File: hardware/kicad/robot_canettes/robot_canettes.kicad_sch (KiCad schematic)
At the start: 0 parts

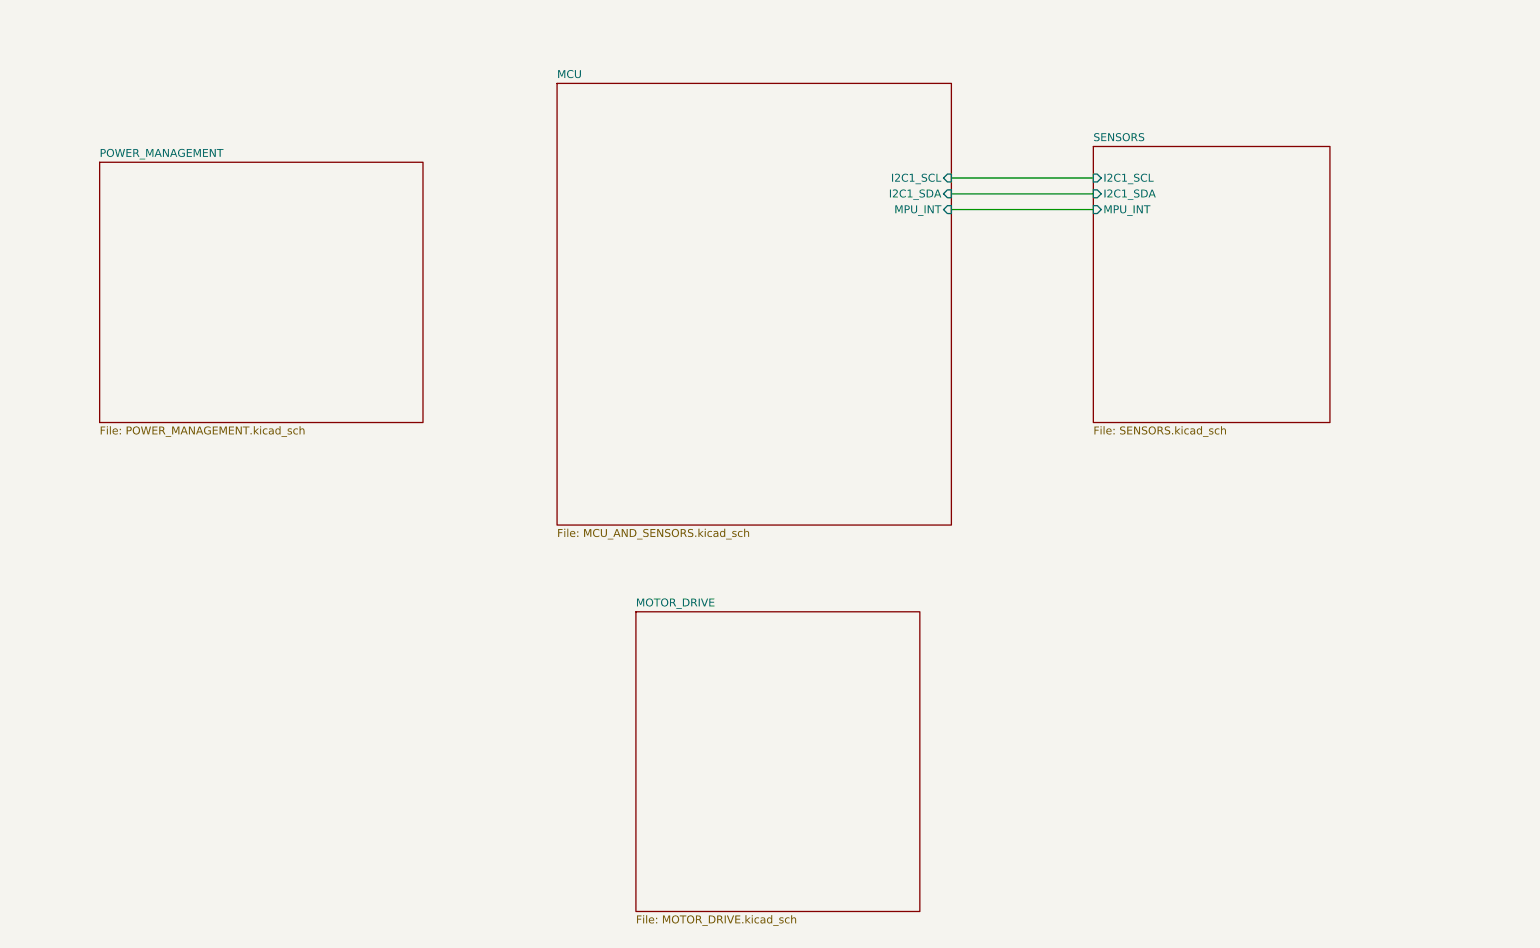
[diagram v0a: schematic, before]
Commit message: MAJ schema MCU/sensors
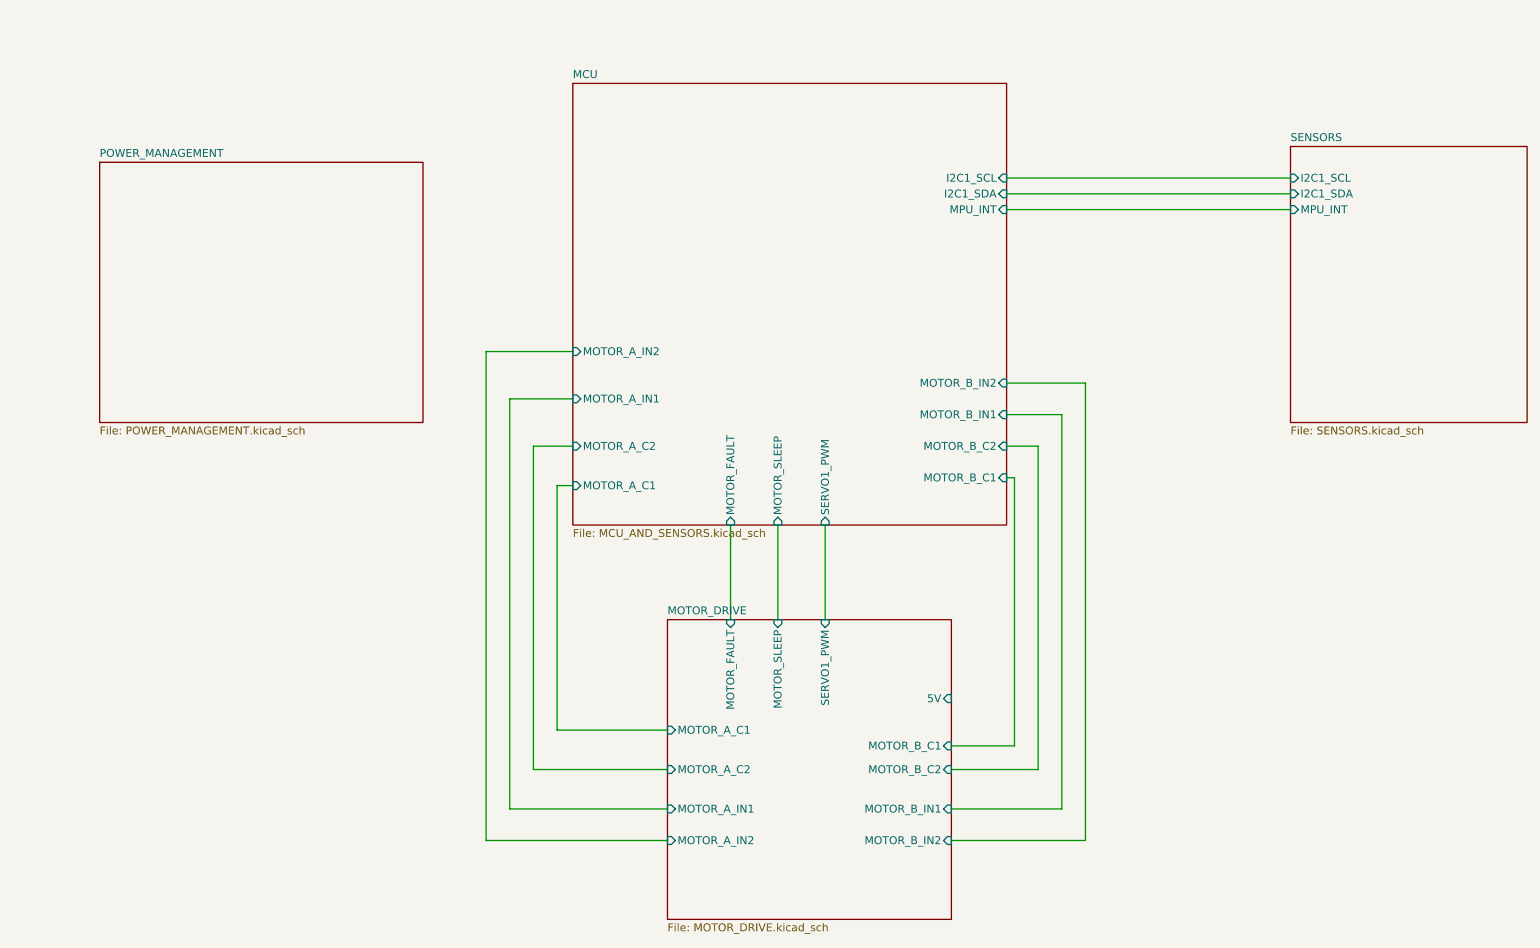
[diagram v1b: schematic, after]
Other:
- sheet MCU ports: added MOTOR_A_C1, MOTOR_A_C2, MOTOR_A_IN1, MOTOR_A_IN2, MOTOR_B_C1, MOTOR_B_C2, MOTOR_B_IN1, MOTOR_B_IN2, MOTOR_FAULT, MOTOR_SLEEP, SERVO1_PWM; removed none
- sheet MOTOR_DRIVE ports: added 5V, MOTOR_A_C1, MOTOR_A_C2, MOTOR_A_IN1, MOTOR_A_IN2, MOTOR_B_C1, MOTOR_B_C2, MOTOR_B_IN1, MOTOR_B_IN2, MOTOR_FAULT, MOTOR_SLEEP, SERVO1_PWM; removed none

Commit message: MAJ connecteur TOF2 (J10) et resistances pull-up
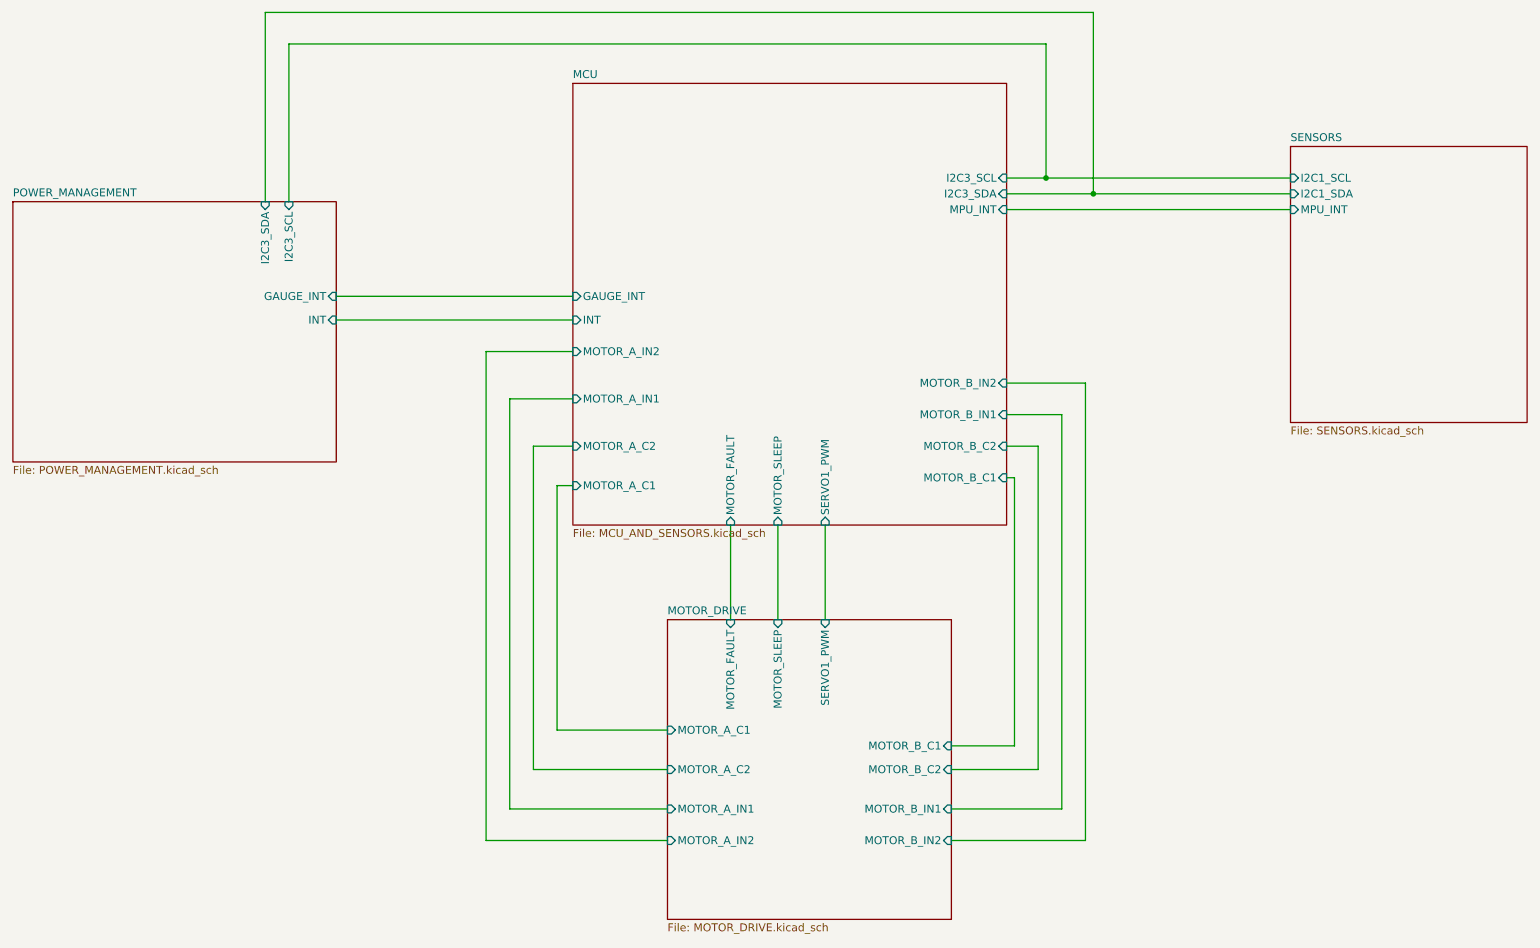
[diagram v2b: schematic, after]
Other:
- sheet MCU ports: added GAUGE_INT, I2C3_SCL, I2C3_SDA, INT; removed I2C1_SCL, I2C1_SDA
- sheet MOTOR_DRIVE ports: added none; removed 5V
- sheet POWER_MANAGEMENT ports: added GAUGE_INT, I2C3_SCL, I2C3_SDA, INT; removed none
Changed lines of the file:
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@@
 	(generator_version "10.0")
 	(paper "A4")
+	(junction
+		(at 205.74 46.99)
+		(diameter 0)
+		(color 0 0 0 0)
+	)
+	(junction
+		(at 198.12 44.45)
+		(diameter 0)
+		(color 0 0 0 0)
+	)
 	(wire
 		(pts
@@
 	(wire
 		(pts
+			(xy 76.2 48.26) (xy 76.2 22.86)
+		)
+		(stroke
+			(width 0)
+			(type default)
+		)
+	)
+	(wire
+		(pts
 			(xy 107.95 72.39) (xy 107.95 151.13)
 		)
@@
 	(wire
 		(pts
+			(xy 205.74 46.99) (xy 237.49 46.99)
+		)
+		(stroke
+			(width 0)
+			(type default)
+		)
+	)
+	(wire
+		(pts
+			(xy 83.82 63.5) (xy 121.92 63.5)
+		)
+		(stroke
+			(width 0)
+			(type default)
+		)
+	)
+	(wire
+		(pts
+			(xy 72.39 17.78) (xy 205.74 17.78)
+		)
+		(stroke
+			(width 0)
+			(type default)
+		)
+	)
+	(wire
+		(pts
 			(xy 154.94 100.33) (xy 154.94 115.57)
 		)
@@
 	(wire
 		(pts
+			(xy 198.12 44.45) (xy 237.49 44.45)
+		)
+		(stroke
+			(width 0)
+			(type default)
+		)
+	)
+	(wire
+		(pts
+			(xy 198.12 22.86) (xy 198.12 44.45)
+		)
+		(stroke
+			(width 0)
+			(type default)
+		)
+	)
+	(wire
+		(pts
 			(xy 121.92 87.63) (xy 115.57 87.63)
 		)
@@
 	(wire
 		(pts
+			(xy 72.39 48.26) (xy 72.39 17.78)
+		)
+		(stroke
+			(width 0)
+			(type default)
+		)
+	)
+	(wire
+		(pts
 			(xy 147.32 100.33) (xy 147.32 115.57)
 		)
@@
 	(wire
 		(pts
+			(xy 76.2 22.86) (xy 198.12 22.86)
+		)
+		(stroke
+			(width 0)
+			(type default)
+		)
+	)
+	(wire
+		(pts
 			(xy 121.92 93.98) (xy 119.38 93.98)
 		)
@@
 	(wire
 		(pts
+			(xy 205.74 17.78) (xy 205.74 46.99)
+		)
+		(stroke
+			(width 0)
+			(type default)
+		)
+	)
+	(wire
+		(pts
 			(xy 200.66 146.05) (xy 182.88 146.05)
 		)
@@
 	(wire
 		(pts
-			(xy 191.77 44.45) (xy 237.49 44.45)
+			(xy 191.77 44.45) (xy 198.12 44.45)
 		)
 		(stroke
@@
 	(wire
 		(pts
-			(xy 191.77 46.99) (xy 237.49 46.99)
+			(xy 191.77 46.99) (xy 205.74 46.99)
+		)
+		(stroke
+			(width 0)
+			(type default)
+		)
+	)
+	(wire
+		(pts
+			(xy 83.82 67.31) (xy 121.92 67.31)
 		)
 		(stroke
@@
 	)
 	(sheet
-		(at 45.72 41.91)
+		(at 31.75 48.26)
 		(size 52.07 41.91)
 		(exclude_from_sim no)
@@
 		)
 		(property "Sheetname" "POWER_MANAGEMENT"
-			(at 45.72 41.1984 0)
+			(at 31.75 47.5484 0)
 			(show_name no)
 			(do_not_autoplace no)
@@
 		)
 		(property "Sheetfile" "POWER_MANAGEMENT.kicad_sch"
-			(at 45.72 84.4046 0)
+			(at 31.75 90.7546 0)
 			(show_name no)
 			(do_not_autoplace no)
@@
 				)
 				(justify left top)
+			)
+		)
+		(pin "GAUGE_INT" input
+			(at 83.82 63.5 0)
+			(effects
+				(font
+					(size 1.27 1.27)
+				)
+				(justify right)
+			)
+		)
+		(pin "I2C3_SCL" input
+			(at 76.2 48.26 90)
+			(effects
+				(font
+					(size 1.27 1.27)
+				)
+				(justify right)
+			)
+		)
+		(pin "I2C3_SDA" input
+			(at 72.39 48.26 90)
+			(effects
+				(font
+					(size 1.27 1.27)
+				)
+				(justify right)
+			)
+		)
+		(pin "INT" input
+			(at 83.82 67.31 0)
+			(effects
+				(font
+					(size 1.27 1.27)
+				)
+				(justify right)
 			)
 		)
@@
 			)
 		)
-		(pin "I2C1_SCL" input
-			(at 191.77 44.45 0)
-			(effects
-				(font
-					(size 1.27 1.27)
-				)
-				(justify right)
-			)
-		)
-		(pin "I2C1_SDA" input
-			(at 191.77 46.99 0)
-			(effects
-				(font
-					(size 1.27 1.27)
-				)
-				(justify right)
-			)
-		)
 		(pin "MPU_INT" input
 			(at 191.77 49.53 0)
@@
 		(pin "SERVO1_PWM" input
 			(at 162.56 100.33 270)
+			(effects
+				(font
+					(size 1.27 1.27)
+				)
+				(justify left)
+			)
+		)
+		(pin "GAUGE_INT" input
+			(at 121.92 63.5 180)
+			(effects
+				(font
+					(size 1.27 1.27)
+				)
+				(justify left)
+			)
+		)
+		(pin "I2C3_SCL" input
+			(at 191.77 44.45 0)
+			(effects
+				(font
+					(size 1.27 1.27)
+				)
+				(justify right)
+			)
+		)
+		(pin "I2C3_SDA" input
+			(at 191.77 46.99 0)
+			(effects
+				(font
+					(size 1.27 1.27)
+				)
+				(justify right)
+			)
+		)
+		(pin "INT" input
+			(at 121.92 67.31 180)
 			(effects
 				(font
@@
 			)
 		)
-		(pin "5V" input
-			(at 182.88 128.27 0)
-			(effects
-				(font
-					(size 1.27 1.27)
-				)
-				(justify right)
-			)
-		)
